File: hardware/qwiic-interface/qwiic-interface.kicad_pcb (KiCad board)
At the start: 4 copper layers, 59.1 x 16.2 mm, 21 parts, among them J1 MOLEX connector, J2 QWIIC Connector, U1 BD9G341EFJ

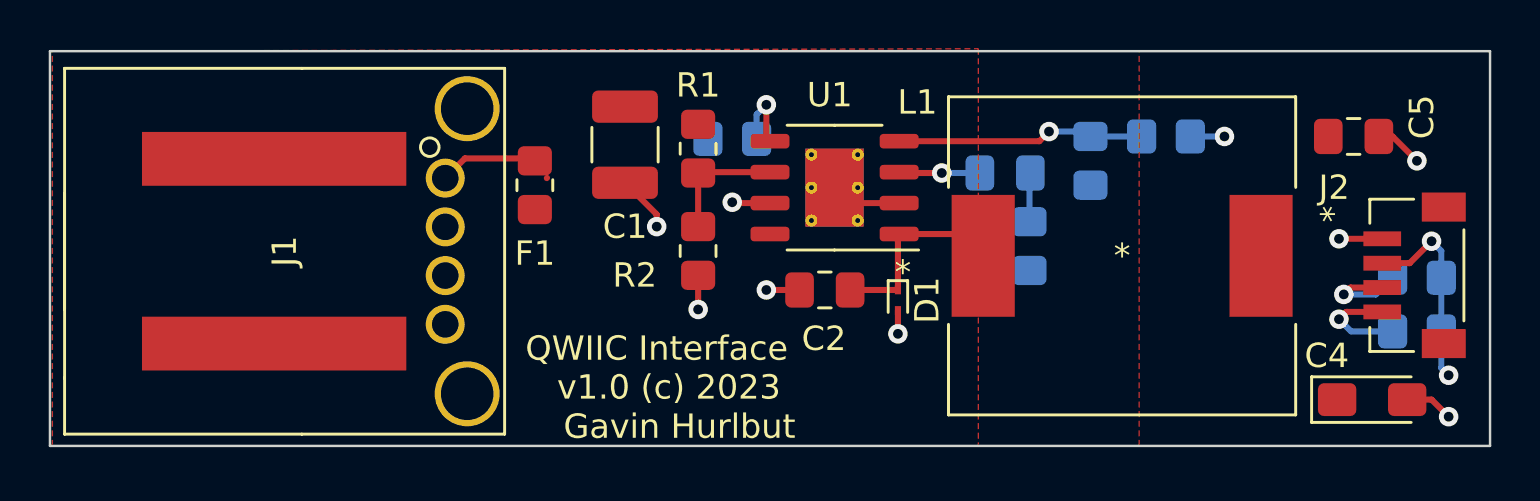
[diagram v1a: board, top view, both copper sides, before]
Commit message: Got rid of TINY diode (0402!?!?), remove USE_USB, put in PicoW
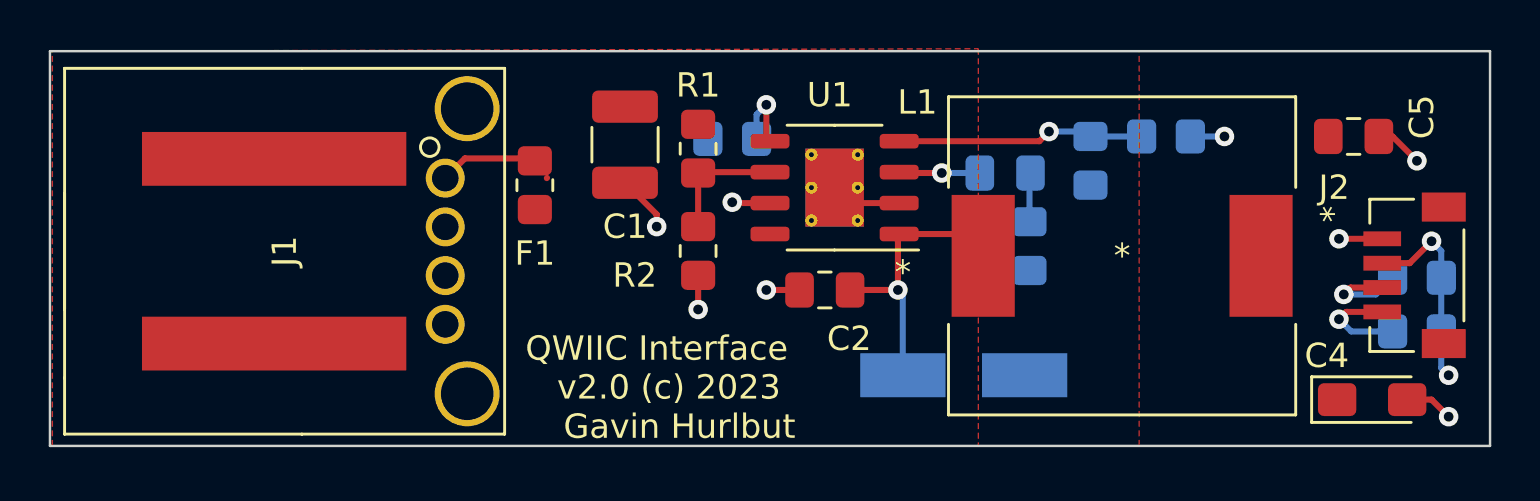
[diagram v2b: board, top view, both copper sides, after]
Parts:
- removed REF**: OSHW-Logo2_7.3x6mm_SilkScreen, Symbol:OSHW-Logo2_7.3x6mm_SilkScreen
- D1: value ACDBQC0130L-HF -> BYS10-35; footprint Diode_SMD:D_SOD-923 -> Diode_SMD:D_SMA_Handsoldering; moved to B.Cu
- moved G*** 16.7 mm to (126.1, 73.2)
- moved D1 4.10 mm to (137.5, 73.1), turned to 0 degrees
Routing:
- net Net-(C2-Pad2): track 8.10 -> 11.7 mm, vias 0 -> 1
- net GND: track 13.4 -> 12.4 mm, vias 6 -> 5
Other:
- board text added: "v2.0 (c) 2023 Gavin Hurlbut"
- board text removed: "v1.0 (c) 2023 Gavin Hurlbut"
